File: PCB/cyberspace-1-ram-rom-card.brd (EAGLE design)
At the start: 100 x 50 mm, 26 parts, among them U1 16V8, U3 16V8, U4 SRAM 32Kx8, U5 ROM 256K, U6 SRAM 32Kx8

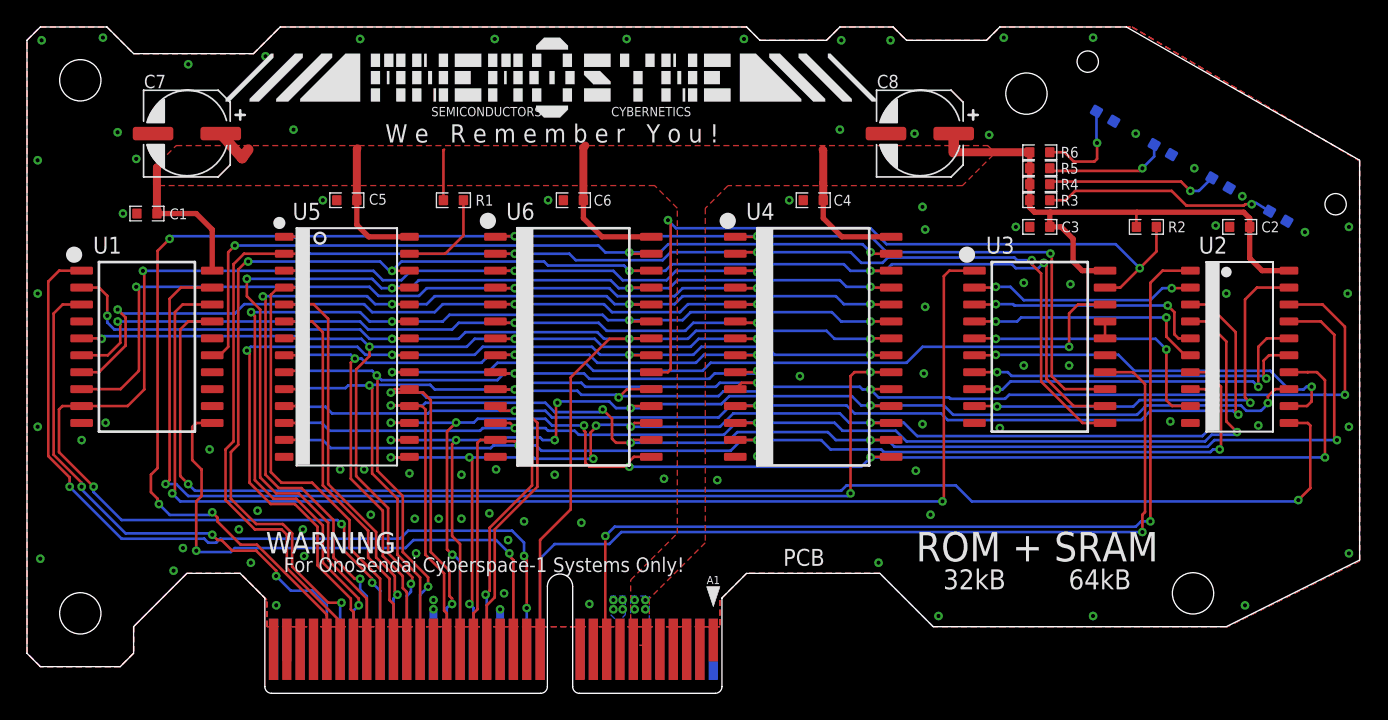
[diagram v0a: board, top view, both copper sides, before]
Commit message: New RamRom using flash chip.
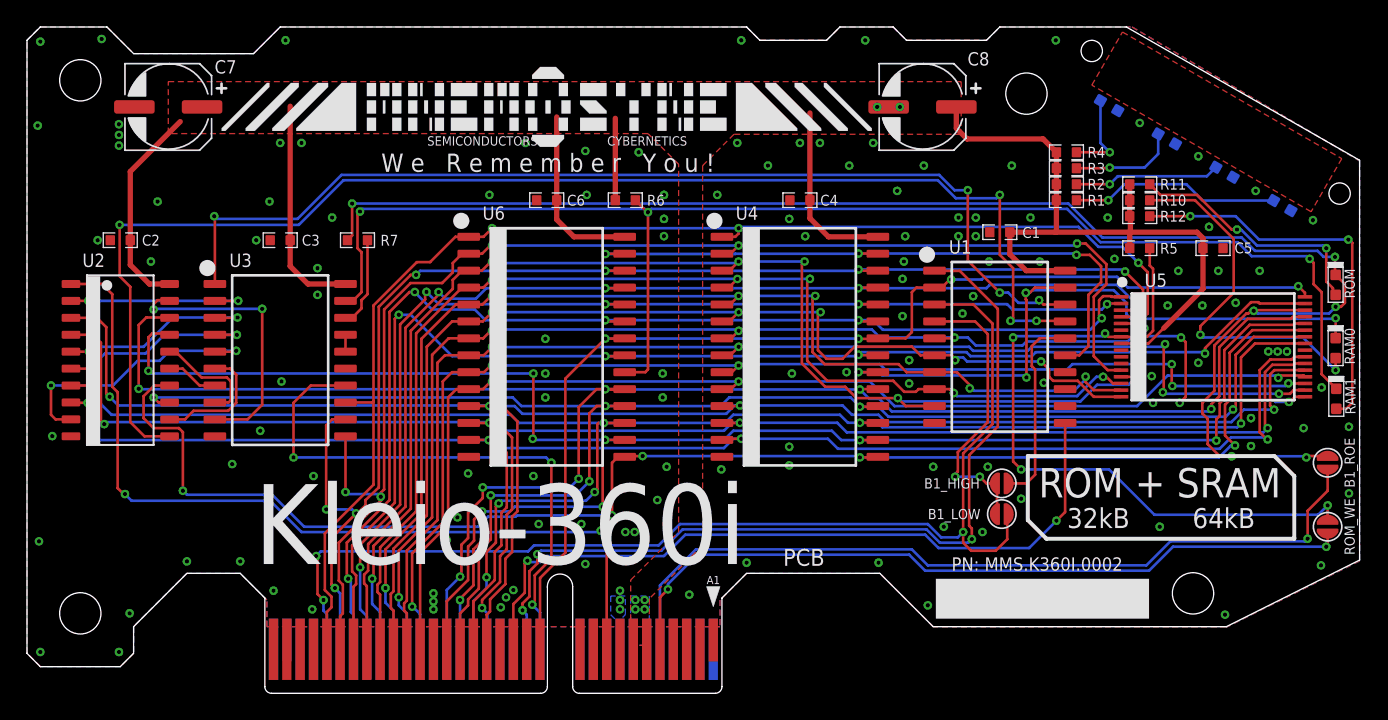
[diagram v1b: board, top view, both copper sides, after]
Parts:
- added B1_HIGH, B1_LOW, B1_ROE, ROM_WE: (no value), rlc:SOLDER_JUMP_60MIL_RND
- added R10, R11, R12: 1.5K, rlc:0603-RES
- added R7: 1K, rlc:0603-RES
- added RAM0, ROM: GRN, led:SMD_0603
- added RAM1: GNR, led:SMD_0603
- R1, R2: value 4.7K -> 470R
- R5, R6: value 470R -> 4.7K
- U5: value ROM 256K -> FLASH 512K x 8; device logic:SO28 -> logic:TSOP32-14X8MM
- moved C2 84.0 mm to (7.00, 34.0)
- moved U2 84.0 mm to (7.00, 25.0)
- moved C5 65.1 mm to (89.0, 33.4), turned to 0 degrees
- moved U5 65.0 mm to (89.0, 26.0)
- moved C1 64.0 mm to (73.0, 34.6)
- moved U1 64.0 mm to (73.0, 26.0)
- moved C3 57.0 mm to (19.0, 34.0)
- moved U3 57.0 mm to (19.0, 25.0)
- moved R1 46.0 mm to (78.0, 37.0)
- moved R6 31.3 mm to (44.9, 37.0)
- moved R5 9.60 mm to (83.5, 33.4)
- moved R2 6.80 mm to (78.0, 38.2)
- moved R3 3.12 mm to (78.0, 39.4)
- moved R4 3.12 mm to (78.0, 40.6)
- moved C7 2.44 mm to (10.6, 44.0)
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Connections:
- new net !B1ROE_PLD: R7.1, U3.18
- new net !ROM_WE: R5.1, ROM_WE.2, U5.7
- new net N$10: PCB.A5, ROM_WE.1
- new net N$7: R11.2, ROM.A
- new net N$8: R12.2, RAM1.A
- new net N$9: B1_ROE.1, PCB.B5
- net !A15: now also B1_HIGH.1
- net !B0: now also B1_HIGH.2, B1_LOW.2
- net !B0E: now also RAM0.K
- net !B1RAE: now also R6.1, RAM1.K; no longer R2.1
- net !B1ROE: now also B1_ROE.2, R7.2, ROM.K, U5.30; no longer U3.18, U5.20
- net !R: now also U5.32; no longer U5.22
- net A0: now also U5.20; no longer U5.10
- net A1: now also U5.19; no longer U5.9
- net A10: now also U5.31; no longer U5.21
- net A11: now also U5.1; no longer U5.23
- net A12: now also U5.12; no longer U5.2
- net A13: now also U5.4; no longer U5.26
- net A14: now also U5.5; no longer U5.1
- net A15: now also B1_LOW.1
- net A2: now also U5.18; no longer U5.8
- net A3: now also U5.17; no longer U5.7
- net A4: now also U5.16; no longer U5.6
- net A5: now also U5.15; no longer U5.5
- net A6: now also U5.14; no longer U5.4
- net A7: now also U5.13; no longer U5.3
- net A8: now also U5.3; no longer U5.25
- net A9: now also U5.2; no longer U5.24
- net D0: now also U5.21; no longer U5.11
- net D1: now also U5.22; no longer U5.12
- net D2: now also U5.23; no longer U5.13
- net D3: now also U5.25; no longer U5.15
- net D4: now also U5.26; no longer U5.16
- net D5: now also U5.27; no longer U5.17
- net D6: now also U5.28; no longer U5.18
- net D7: now also U5.29; no longer U5.19
- net GND: now also U5.10, U5.11, U5.24, U5.6, U5.9; no longer U5.14
- net N$2: now also R1.1; no longer R3.1
- net N$3: now also R2.1; no longer R4.1
- net N$4: now also R10.2, RAM0.A; no longer R1.1, U5.27
- net N$5: now also R3.1; no longer R5.1
- net N$6: now also R4.1; no longer R6.1
- net VCC: now also R10.1, R11.1, R12.1, U5.8; no longer U5.28
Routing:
- net N$9: track 0.00 -> 61.7 mm, vias 0 -> 1
- net N$10: track 0.00 -> 57.7 mm, vias 0 -> 2
- net !B1ROE: track 58.9 -> 114.7 mm, vias 2 -> 6
- net !ROM_WE: track 0.00 -> 53.2 mm, vias 0 -> 4
- net !B1RAE: track 56.7 -> 106.4 mm, vias 2 -> 3
- net A15: track 42.0 -> 85.6 mm
- net D3: track 89.1 -> 127.3 mm, vias 8 -> 7
- net !B0E: track 81.4 -> 49.9 mm, vias 3 -> 4
- net A2: track 63.3 -> 94.1 mm, vias 4 -> 5
- net D4: track 93.7 -> 123.4 mm, vias 7 -> 6
- net N$8: track 0.00 -> 29.4 mm, vias 0 -> 2
- net A1: track 62.0 -> 90.1 mm, vias 5 -> 6
- net A0: track 60.9 -> 88.0 mm, vias 4 -> 3
- net A14: track 124.6 -> 98.9 mm, vias 7 -> 3
- net D2: track 99.6 -> 124.7 mm
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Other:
- board text added: "For OnoSendai Cyberspace-1 System Only!"
- board text added: "Kleio-360i"
- board text added: "PN: MMS.K360I.0002"
- board text removed: "For OnoSendai Cyberspace-1 Systems Only!"
